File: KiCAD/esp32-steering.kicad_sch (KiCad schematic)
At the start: 26 parts, among them J1 Conn_01x02, SW1 RotaryEncoder_Switch_MP, SW2 RotaryEncoder_Switch_MP, SW4 SW_SPST, SW5 SW_SPST

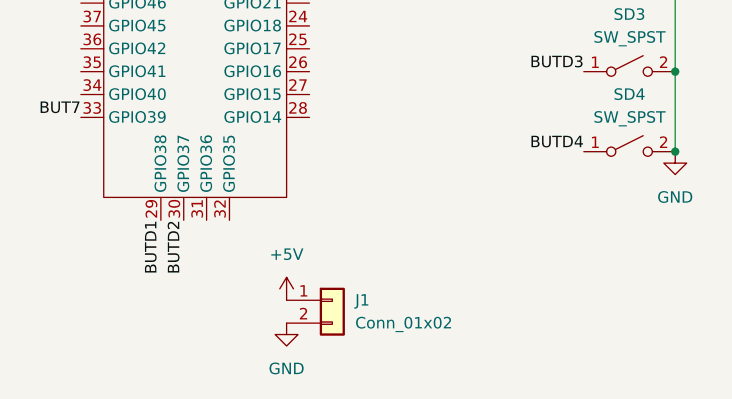
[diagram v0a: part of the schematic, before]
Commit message: correct footprint and pcb design for battery connections
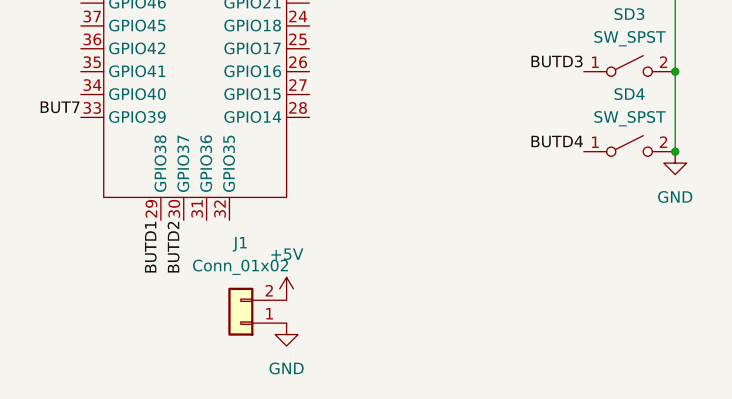
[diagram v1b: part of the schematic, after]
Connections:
- net +5V: now also J1.2 (Pin_2); no longer J1.1 (Pin_1)
- net GND: now also J1.1 (Pin_1); no longer J1.2 (Pin_2)
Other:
- moved on the sheet: J1
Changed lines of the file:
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@@
 	(symbol
 		(lib_id "Connector_Generic:Conn_01x02")
-		(at 69.85 125.73 0)
+		(at 59.69 128.27 180)
 		(unit 1)
 		(exclude_from_sim no)
@@
 		(fields_autoplaced yes)
 		(property "Reference" "J1"
-			(at 72.39 125.7299 0)
+			(at 59.69 119.38 0)
 			(effects
 				(font
 					(size 1.27 1.27)
 				)
-				(justify left)
 			)
 		)
 		(property "Value" "Conn_01x02"
-			(at 72.39 128.2699 0)
+			(at 59.69 121.92 0)
 			(effects
 				(font
 					(size 1.27 1.27)
 				)
-				(justify left)
 			)
 		)
 		(property "Footprint" "userFootprints:JST_XH_S2B-XH-A-1_1x02_P2.50mm_Horizontal-short"
-			(at 69.85 125.73 0)
+			(at 59.69 128.27 0)
 			(effects
 				(font
@@
 		)
 		(property "Datasheet" "~"
-			(at 69.85 125.73 0)
+			(at 59.69 128.27 0)
 			(effects
 				(font
@@
 		)
 		(property "Description" "Generic connector, single row, 01x02, script generated (kicad-library-utils/schlib/autogen/connector/)"
-			(at 69.85 125.73 0)
+			(at 59.69 128.27 0)
 			(effects
 				(font
